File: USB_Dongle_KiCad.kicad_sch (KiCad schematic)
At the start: 39 parts, among them SW1 SW_SPDT, U1 ESDA14V2-2BF3, U2 USBULC6-2M6, Y1 24MHz / 10pF / 20ppm

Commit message: Tiny updates in the schematics
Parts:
- added R1: 12k, symbol Device:R_Small_US
- FB?: value 120R@100MHz -> 120@100MHz
- SW1: value SW_SPDT -> PCM12SMTR; footprint (none) -> Button_Switch_SMD:SW_SPDT_PCM12
- SW?: value SW_Push -> KMR223G LFG
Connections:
- net GND: now also U?.E2 (VB_REF_FAULT), R1.1
- net SDMMC_CLK: now also J?.5 (CLK)
- net SDMMC_D0: now also J?.7 (DAT0)
- net SDMMC_D1: now also J?.8 (DAT1)
- net SDMMC_D2: now also J?.1 (DAT2)
- net SDMMC_D3: now also J?.2 (CD/DAT3)
- net at U?.C2 (RREF): now also R1.2
- no-connect marks 7 -> 8
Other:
- note added: "CX2016SA24000F0FLLG1"
- note added: "Tol.=1%"
- company: 2SAYLE -> 2sayle
- title: USB Secure Dongle -> USB Dongle
- moved on the sheet: C2, C3, Y1

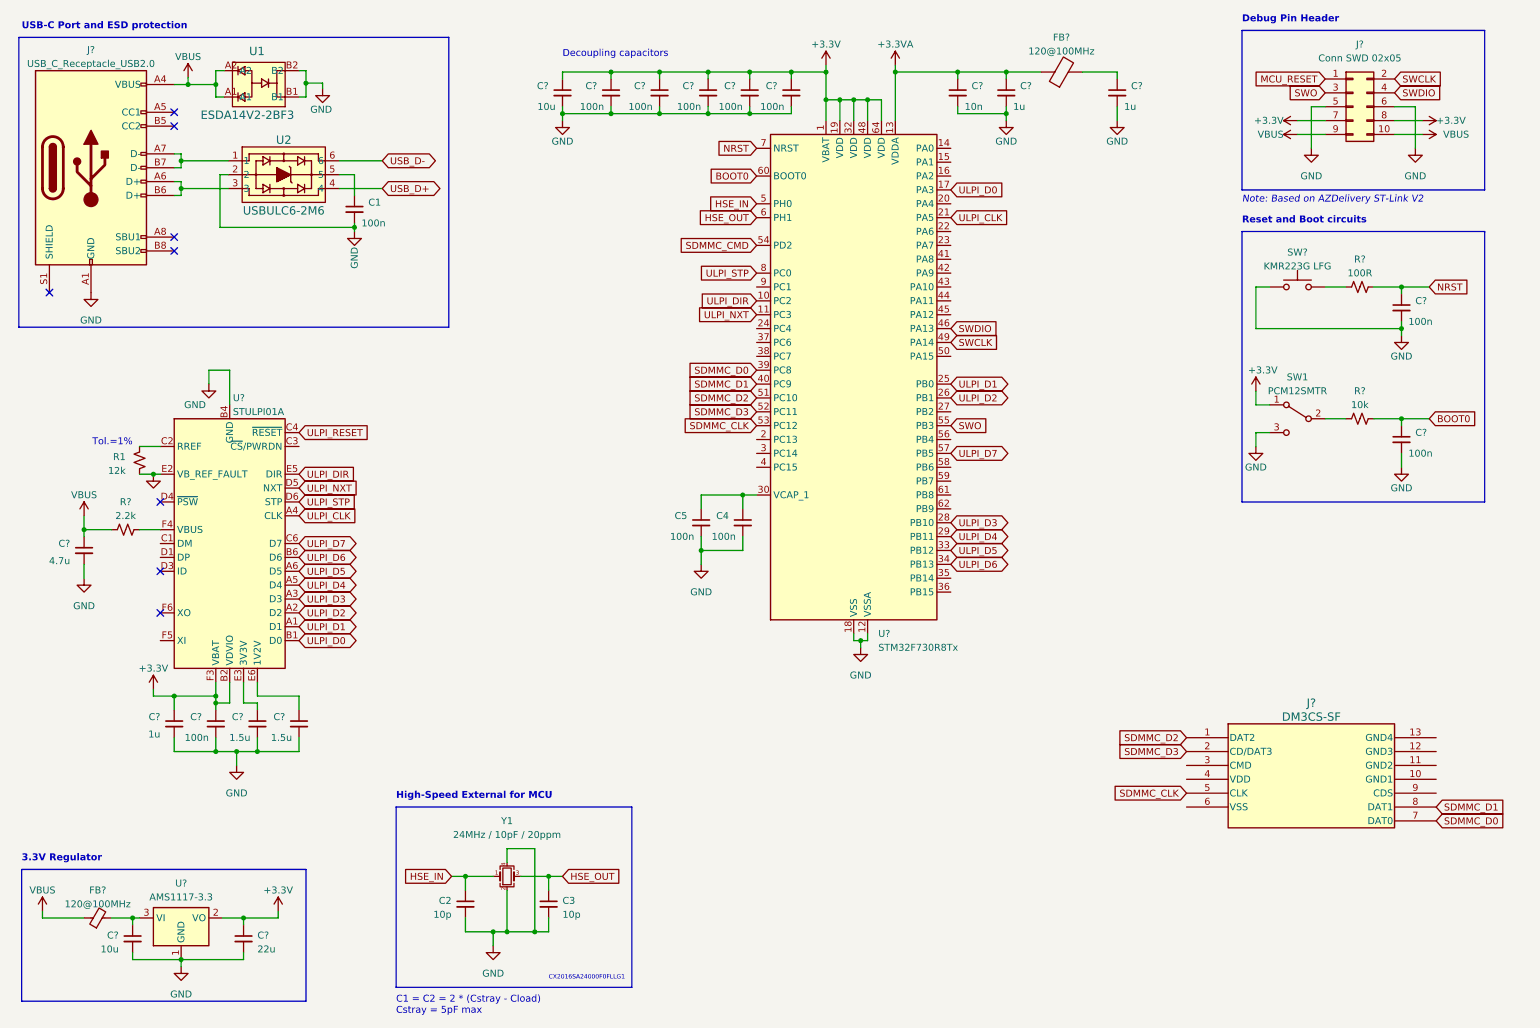
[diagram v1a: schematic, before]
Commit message: Added: New microSD component
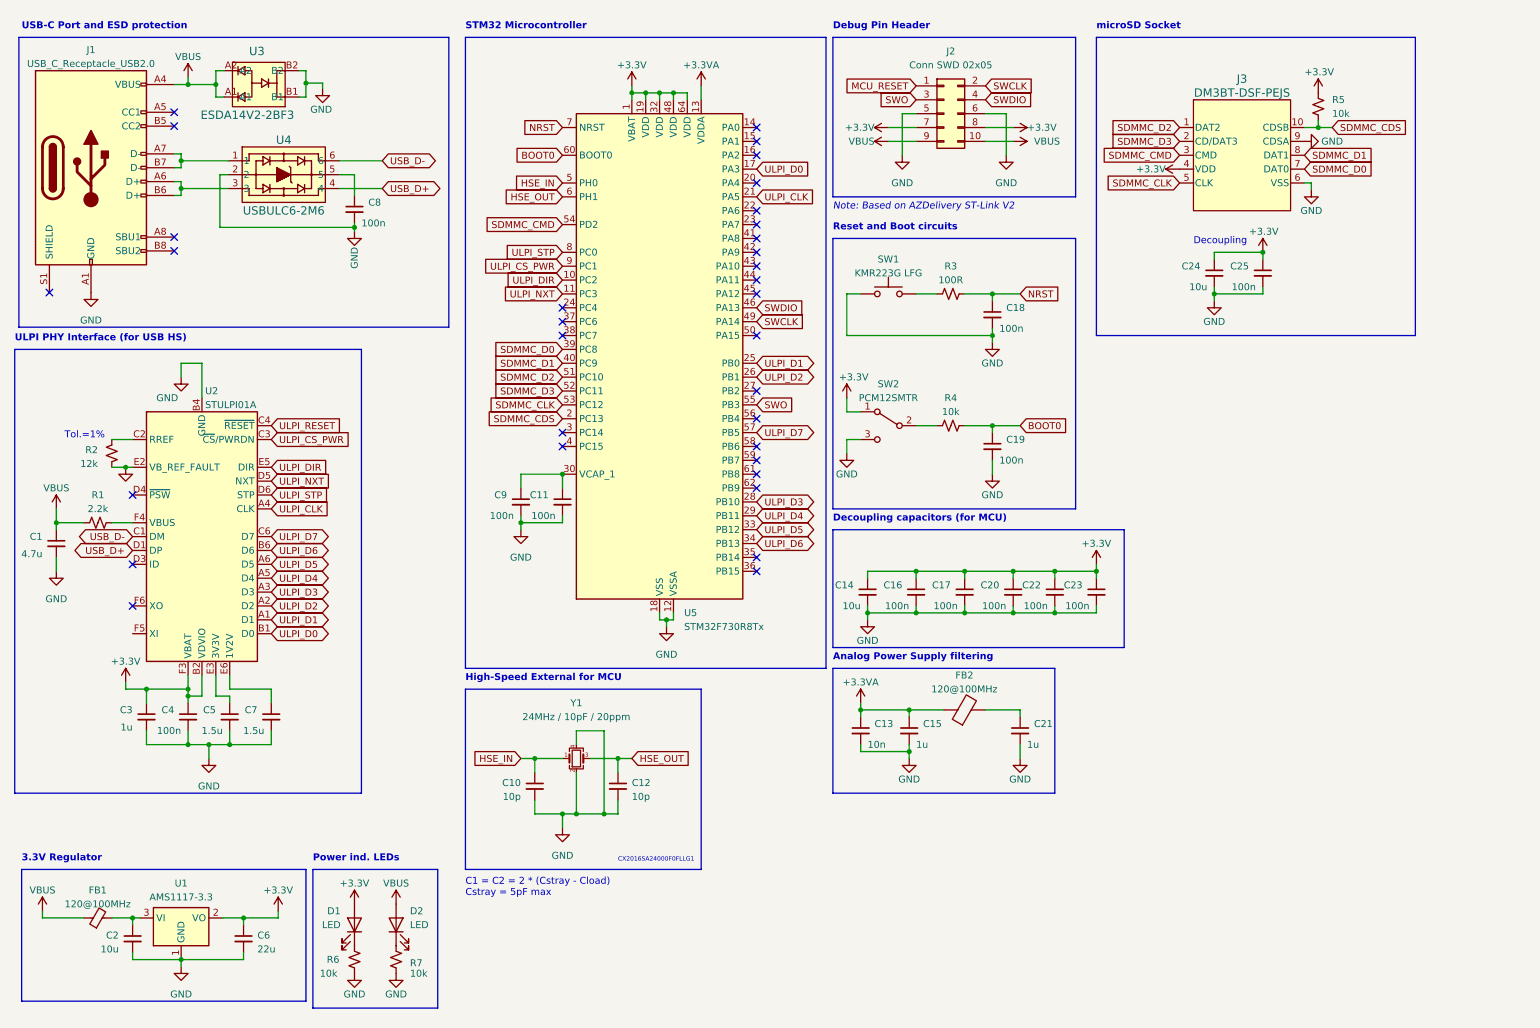
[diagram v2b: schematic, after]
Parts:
- removed J?: DM3CS-SF, fplibs:DM3CS-SF_HIR, symbol libs:DM3CS-SF
- added C24: 10u, symbol Device:C_Small
- added C25: 100n, symbol Device:C_Small
- added D1, D2: LED, symbol Device:LED
- added J3: DM3BT-DSF-PEJS, fplibs:DM3BT-DSF-PEJS_HIR, symbol libs:DM3BT-DSF-PEJS
- added R5, R6, R7: 10k, symbol Device:R_Small_US
- gave numbers to parts that had none: 29
- renumbered C2 to C10, C4 to C11, C3 to C12, C1 to C8, C5 to C9, R1 to R2, SW1 to SW2, U1 to U3, U2 to U4
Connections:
- net +3.3V: now also C24.1, C25.1, D1.2 (A), J3.4 (VDD), R5.2
- net GND: now also C24.2, C25.2, J3.6 (VSS), J3.9 (CDSA), R6.2, R7.2
- net SDMMC_CLK: now also J3.5 (CLK)
- net SDMMC_CMD: now also J3.3 (CMD)
- net SDMMC_D0: now also J3.7 (DAT0)
- net SDMMC_D1: now also J3.8 (DAT1)
- net SDMMC_D2: now also J3.1 (DAT2)
- net SDMMC_D3: now also J3.2 (CD/DAT3)
- net USB_D+: now also U2.D1 (DP)
- net USB_D-: now also U2.C1 (DM)
- net VBUS: now also D2.2 (A)
- net SDMMC_CDS: now reaches U5.2 (PC13)
- net SDMMC_CDS: now also J3.10 (CDSB), R5.1
- net ULPI_CS_PWR: now reaches U5.9 (PC1)
- net ULPI_CS_PWR: now also U2.C3 (~{CS}/PWRDN)
- new net: D1.1 (K), R6.1
- new net: D2.1 (K), R7.1
- no-connect marks 8 -> 33
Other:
- note added: "Analog Power Supply filtering"
- note added: "Decoupling"
- note added: "Decoupling capacitors (for MCU)"
- note added: "Power ind. LEDs"
- note added: "STM32 Microcontroller"
- note added: "ULPI PHY Interface (for USB HS)"
- note added: "microSD Socket"
- note removed: "Decoupling capacitors"
- moved on the sheet: C1, C10, C11, C12, C13, C14, C15, C16, C17, C18, C19, C20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

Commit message: Added: Clock oscillator for ULPI
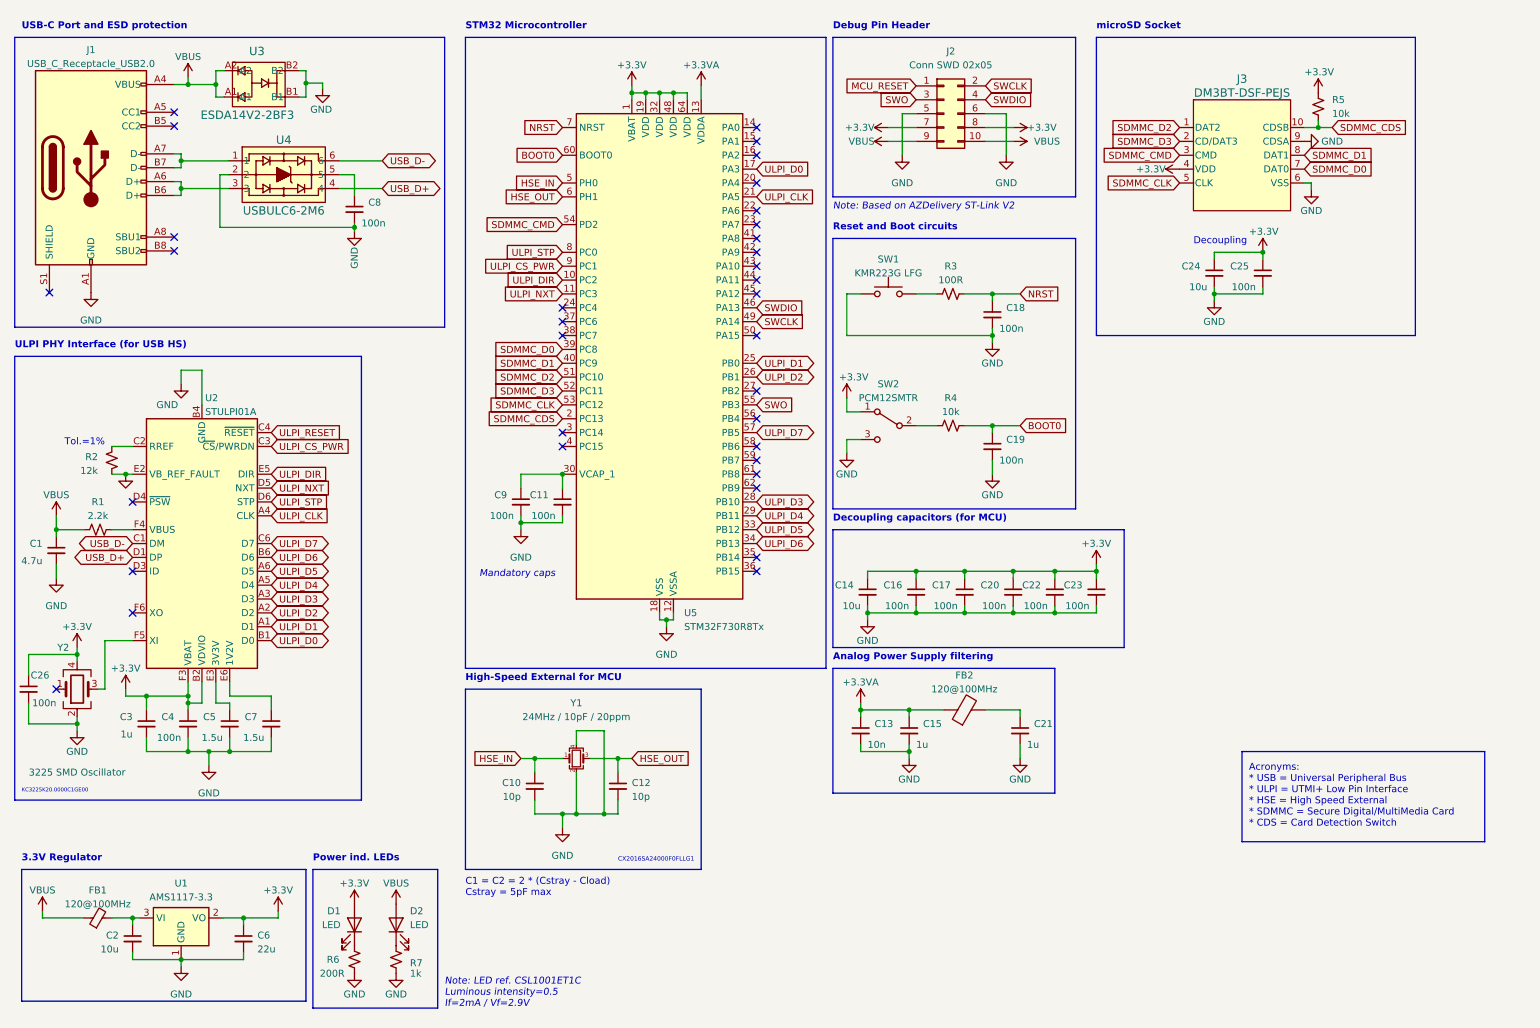
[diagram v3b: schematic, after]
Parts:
- added C26: 100n, symbol Device:C_Small
- added Y2: 3225 SMD Oscillator, Crystal:Crystal_SMD_3225-4Pin_3.2x2.5mm, symbol Device:Crystal_GND24
- D1, D2: footprint (none) -> LED_SMD:LED_0603_1608Metric
- R6: value 10k -> 200R
- R7: value 10k -> 1k
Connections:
- net +3.3V: now also C26.1, Y2.4
- net GND: now also C26.2, Y2.2
- net at U2.F5 (XI): now also Y2.3
- no-connect marks 33 -> 34
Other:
- note added: "Acronyms: * USB = Universal Peripheral Bus * ULPI = UTMI+ Low Pin Interface * HSE = High Speed External * SDMMC = Secure Digital/MultiMedia Card * CDS = Card Detection Switch"
- note added: "KC3225K20.0000C1GE00"
- note added: "Mandatory caps"
- note added: "Note: LED ref. CSL1001ET1C Luminous intensity=0.5 If=2mA / Vf=2.9V"
- moved on the sheet: C1, C3, C4, C5, C7, R1, R2, U2

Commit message: Added: Pull-down resistors for CCx pins (USB-C port)
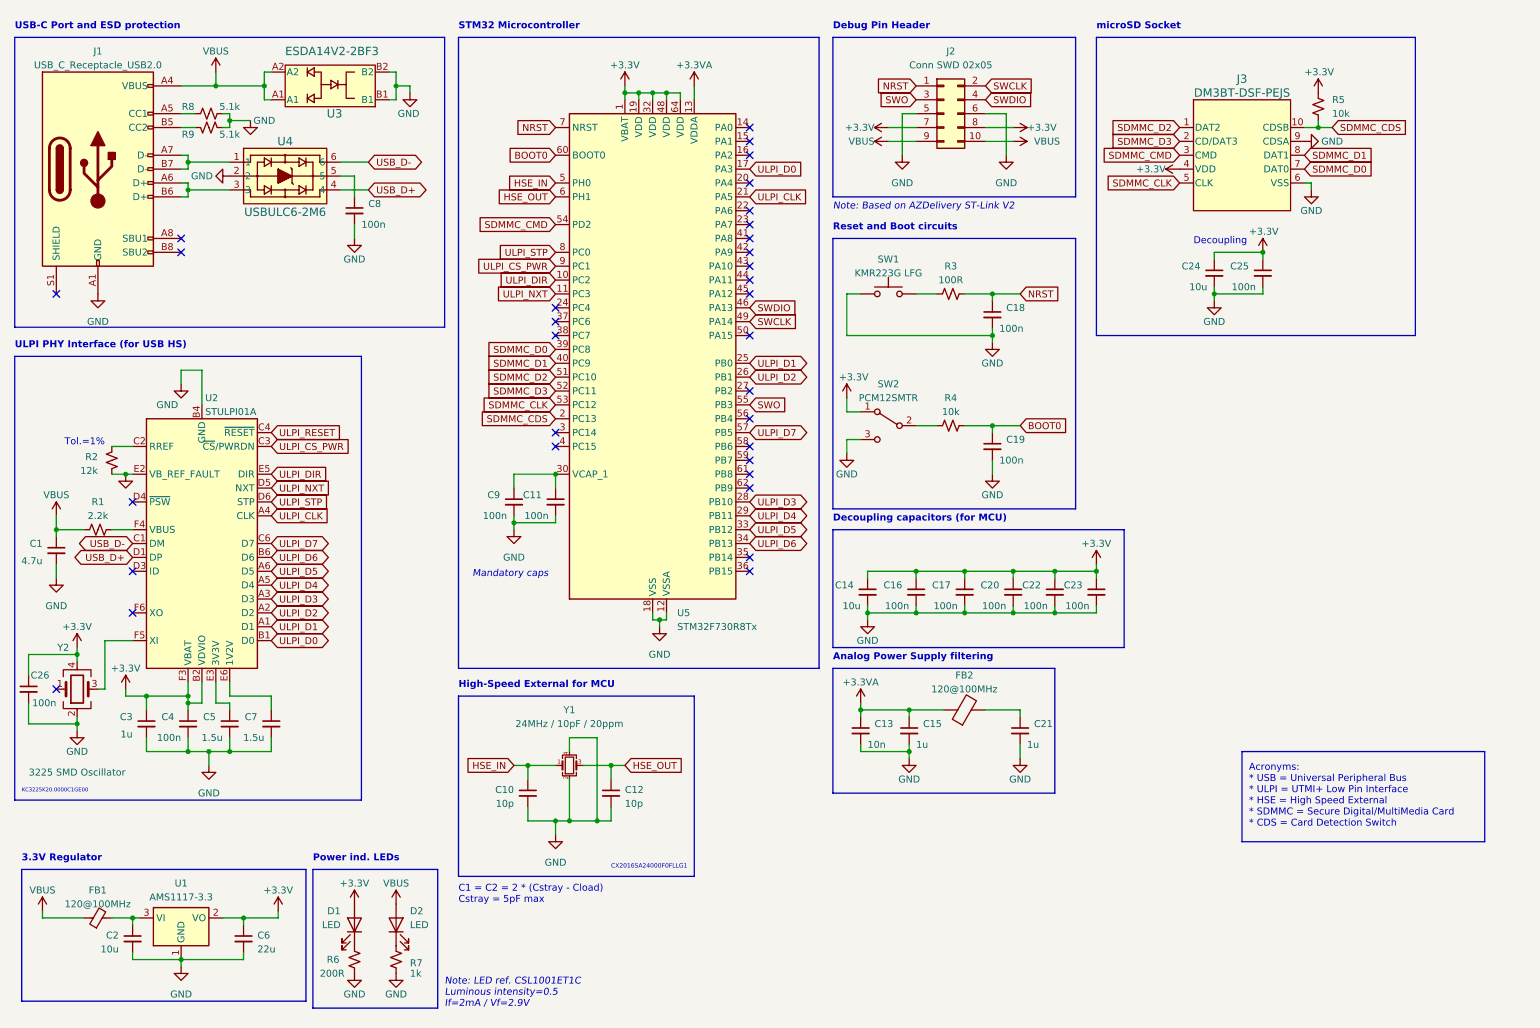
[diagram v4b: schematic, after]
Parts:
- added R8, R9: 5.1k, symbol Device:R_Small_US
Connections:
- net MCU_RESET is gone; now on net NRST: J2.1 (Pin_1)
- net GND: now also R8.2, R9.2
- net at J1.A5 (CC1): now also R8.1
- net at J1.B5 (CC2): now also R9.1
- no-connect marks 34 -> 32
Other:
- moved on the sheet: C10, C11, C12, C9, J1, U3, U5, Y1

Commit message: Executed DRC and ignored irrelevant warnings
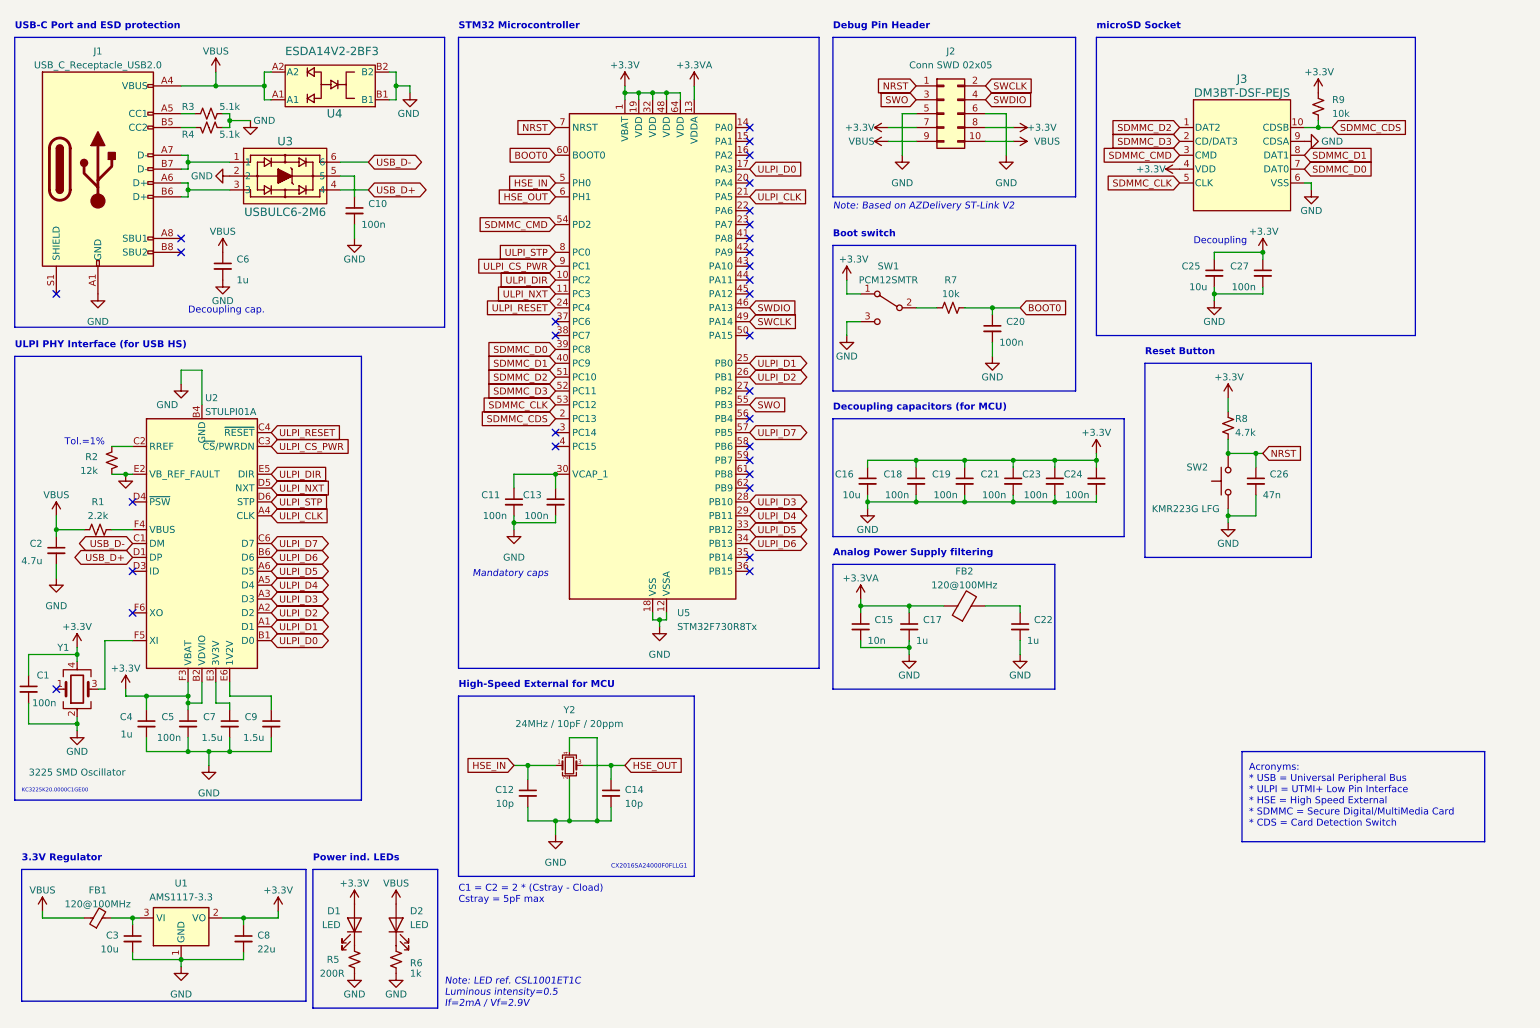
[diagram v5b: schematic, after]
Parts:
- removed C18: 100n, symbol Device:C_Small
- removed R3: 100R, symbol Device:R_Small_US
- removed SW1: KMR223G LFG, Button_Switch_SMD:SW_Push_1P1T_NO_CK_KMR2, symbol Switch:SW_Push
- added C26: 47n, symbol Device:C_Small
- added C6: 1u, symbol Device:C_Small
- added R8: 4.7k, symbol Device:R_Small_US
- added SW2: KMR223G LFG, Button_Switch_SMD:SW_Push_1P1T_NO_CK_KMR2, symbol Switch:SW_Push
- renumbered C26 to C1, C8 to C10, C9 to C11, C10 to C12, C11 to C13, C12 to C14, C13 to C15, C14 to C16, C15 to C17, C16 to C18, C17 to C19, C1 to C2, C19 to C20, C20 to C21, C21 to C22, C22 to C23, C23 to C24, C24 to C25, C25 to C27, C2 to C3, C3 to C4, C4 to C5, C5 to C7, C6 to C8, C7 to C9, R8 to R3, R9 to R4, R6 to R5, R7 to R6, R4 to R7, R5 to R9, SW2 to SW1, U4 to U3, U3 to U4, Y2 to Y1, Y1 to Y2
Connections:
- net +3.3V: now also R8.1
- net GND: now also C26.2, C6.2, SW2.1
- net NRST: now also C26.1, R8.2, SW2.2
- net ULPI_RESET: now also U5.24 (PC4)
- net VBUS: now also C6.1
- no-connect marks 32 -> 31
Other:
- note added: "Boot switch"
- note added: "Decoupling cap."
- note added: "Reset Button"
- note removed: "Reset and Boot circuits"
- moved on the sheet: C15, C16, C17, C18, C19, C20, C21, C22, C23, C24, FB2, R7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
